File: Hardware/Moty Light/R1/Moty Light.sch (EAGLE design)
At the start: 11 parts, among them T1 2SC1815

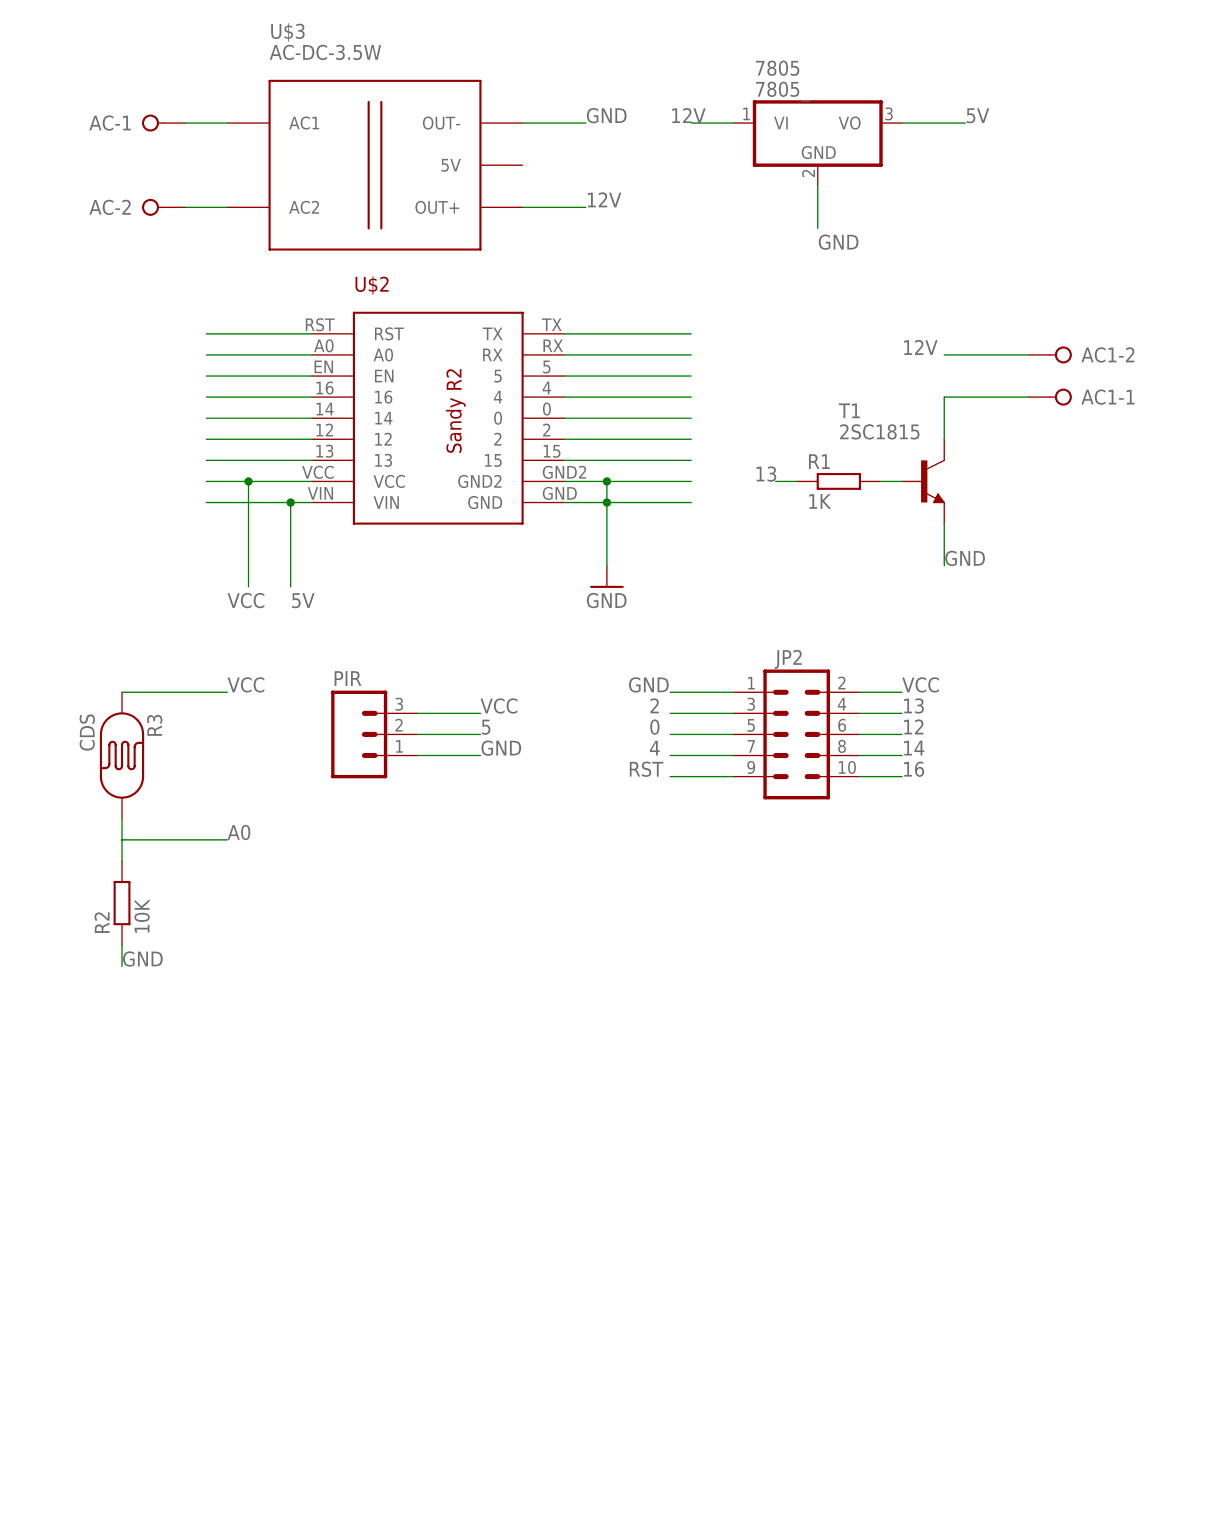
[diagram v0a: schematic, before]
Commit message: Update design for Moty Light
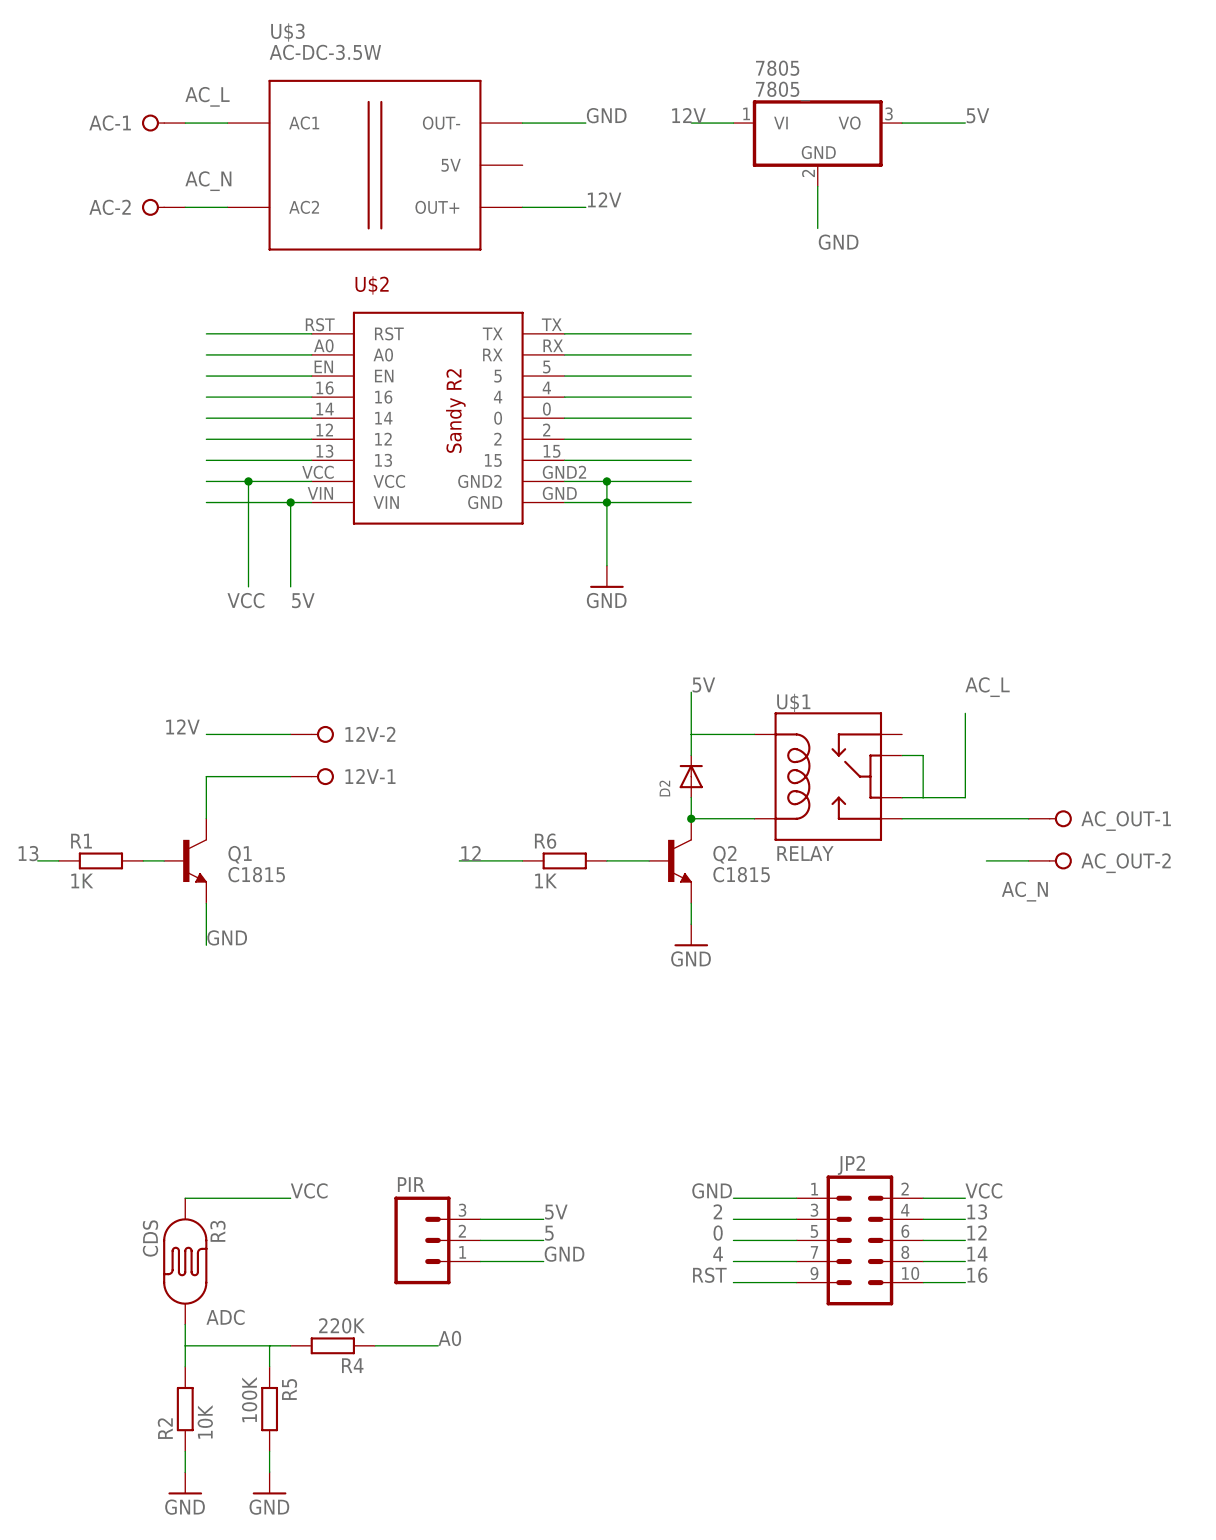
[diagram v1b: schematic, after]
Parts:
- removed AC1: (no value), con-wago-508:W237-02P
- removed T1: 2SC1815, transistor:2SC1815
- added 12V, AC_OUT: (no value), con-wago-508:W237-02P
- added D2: (no value), adafruit:DIODESMA
- added Q1, Q2: C1815, SparkFun-DiscreteSemi:TRANSISTOR_NPNMMBT2222A
- added R4: 220K, rcl:R-EU_R0805
- added R5: 100K, rcl:R-EU_R0805
- added R6: 1K, rcl:R-EU_R0805
- added U$1: RELAY, My Eagle Lib:MINIATURE_RELAY_JRC_21F
- R3: device SparkFun-Sensors:PHOTOCELLPTH -> SparkFun-Sensors:PHOTOCELL
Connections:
- new net ADC: R2.2, R3.P$2, R4.2, R5.1
- new net N$3: D2.A, Q2.C, U$1.COIL2
- new net N$4: Q2.B, R6.2
- new net N$8: AC_OUT-1.KL, U$1.NO
- net 12: now also R6.1
- net 12V: now also 12V-2.KL; no longer AC1-2.KL
- net 5V: now also D2.C, PIR.3, U$1.COIL1
- net A0: now also R4.1; no longer R2.2, R3.P$2
- net AC_L: now also U$1.COM1, U$1.COM2
- net AC_N: now also AC_OUT-2.KL
- net GND: now also Q1.E, Q2.E, R5.2; no longer T1.E
- net N$1: now also 12V-1.KL, Q1.C; no longer AC1-1.KL, T1.C
- net N$7: now also Q1.B; no longer T1.B
- net VCC: no longer PIR.3
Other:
- moved on the sheet: JP2, PIR, R1, R2, R3
